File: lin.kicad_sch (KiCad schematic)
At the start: 11 parts, among them J3 Screw_Terminal_01x03, U5 TJA1029T

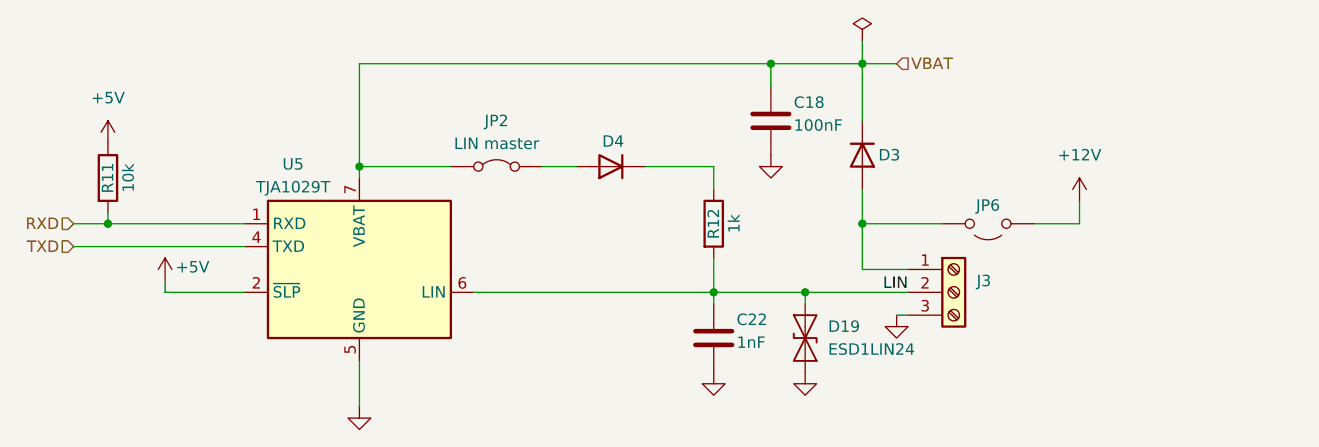
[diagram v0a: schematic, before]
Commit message: Added power diodes
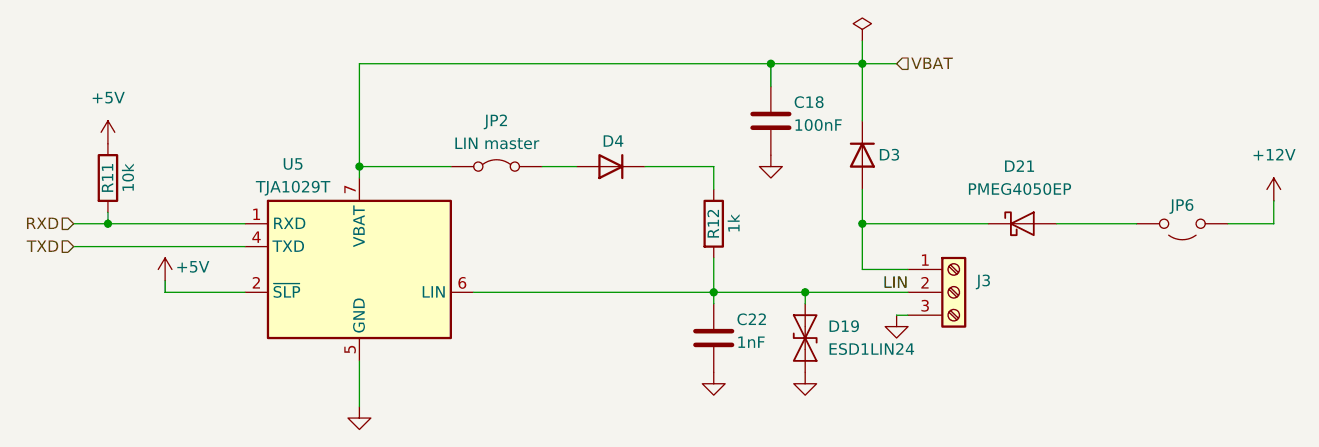
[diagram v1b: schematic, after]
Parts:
- added D21: PMEG4050EP, Diode_SMD:Nexperia_CFP3_SOD-123W, symbol Diode:PMEG4010ER
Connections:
- net at D3.2 (A), J3.1 (Pin_1): now also D21.1 (K); no longer JP6.2 (B)
- new net: D21.2 (A), JP6.2 (B)
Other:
- moved on the sheet: JP6
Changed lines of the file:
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@@
 	(wire
 		(pts
-			(xy 200.66 93.98) (xy 195.58 93.98)
+			(xy 222.25 93.98) (xy 217.17 93.98)
 		)
 		(stroke
@@
 	(wire
 		(pts
-			(xy 200.66 91.44) (xy 200.66 93.98)
+			(xy 222.25 91.44) (xy 222.25 93.98)
 		)
 		(stroke
@@
 	(wire
 		(pts
-			(xy 176.53 93.98) (xy 185.42 93.98)
+			(xy 198.12 93.98) (xy 207.01 93.98)
+		)
+		(stroke
+			(width 0)
+			(type default)
+		)
+	)
+	(wire
+		(pts
+			(xy 176.53 93.98) (xy 190.5 93.98)
 		)
 		(stroke
@@
 	)
 	(symbol
+		(lib_id "Diode:PMEG4010ER")
+		(at 194.31 93.98 0)
+		(unit 1)
+		(exclude_from_sim no)
+		(in_bom yes)
+		(on_board yes)
+		(dnp no)
+		(fields_autoplaced yes)
+		(property "Reference" "D21"
+			(at 193.9925 87.63 0)
+			(effects
+				(font
+					(size 1.27 1.27)
+				)
+			)
+		)
+		(property "Value" "PMEG4050EP"
+			(at 193.9925 90.17 0)
+			(effects
+				(font
+					(size 1.27 1.27)
+				)
+			)
+		)
+		(property "Footprint" "Diode_SMD:Nexperia_CFP3_SOD-123W"
+			(at 194.31 98.425 0)
+			(effects
+				(font
+					(size 1.27 1.27)
+				)
+				(hide yes)
+			)
+		)
+		(property "Datasheet" "https://assets.nexperia.com/documents/data-sheet/PMEG4010ER.pdf"
+			(at 194.31 93.98 0)
+			(effects
+				(font
+					(size 1.27 1.27)
+				)
+				(hide yes)
+			)
+		)
+		(property "Description" "40V, 1A low Vf MEGA Schottky barrier rectifier, SOD-123W"
+			(at 194.31 93.98 0)
+			(effects
+				(font
+					(size 1.27 1.27)
+				)
+				(hide yes)
+			)
+		)
+		(pin "2"
+		)
+		(pin "1"
+		)
+		(instances
+			(project ""
+				(path "/e6cf11d6-0152-4d84-a82a-9e2d93966152/31c6b4ae-10a2-4f10-a591-5579630fa60e"
+					(reference "D22")
+					(unit 1)
+				)
+				(path "/e6cf11d6-0152-4d84-a82a-9e2d93966152/7747294f-2018-4c44-a2cb-fbe0ffa31304"
+					(reference "D24")
+					(unit 1)
+				)
+				(path "/e6cf11d6-0152-4d84-a82a-9e2d93966152/a2f7cee2-a97f-4885-9036-e6c309dcb8d0"
+					(reference "D23")
+					(unit 1)
+				)
+				(path "/e6cf11d6-0152-4d84-a82a-9e2d93966152/ce397451-b7a0-48ce-ab00-72bbf812467b"
+					(reference "D21")
+					(unit 1)
+				)
+			)
+		)
+	)
+	(symbol
 		(lib_id "power:PWR_FLAG")
 		(at 176.53 73.66 0)
@@
 	(symbol
 		(lib_id "Jumper:Jumper_2_Open")
-		(at 190.5 93.98 180)
+		(at 212.09 93.98 180)
 		(unit 1)
 		(exclude_from_sim yes)
@@
 		(dnp no)
 		(property "Reference" "JP6"
-			(at 190.5 91.948 0)
+			(at 212.09 91.948 0)
 			(effects
 				(font
@@
 		)
 		(property "Value" "Jumper_2_Open"
-			(at 190.5 91.44 0)
+			(at 212.09 91.44 0)
 			(effects
 				(font
@@
 		)
 		(property "Footprint" "TestPoint:TestPoint_2Pads_Pitch2.54mm_Drill0.8mm"
-			(at 190.5 93.98 0)
+			(at 212.09 93.98 0)
 			(effects
 				(font
@@
 		)
 		(property "Datasheet" "~"
-			(at 190.5 93.98 0)
+			(at 212.09 93.98 0)
 			(effects
 				(font
@@
 		)
 		(property "Description" "Jumper, 2-pole, open"
-			(at 190.5 93.98 0)
+			(at 212.09 93.98 0)
 			(effects
 				(font
@@
 	(symbol
 		(lib_id "power:+12V")
-		(at 200.66 91.44 0)
+		(at 222.25 91.44 0)
 		(unit 1)
 		(exclude_from_sim no)
@@
 		(fields_autoplaced yes)
 		(property "Reference" "#PWR083"
-			(at 200.66 95.25 0)
+			(at 222.25 95.25 0)
 			(effects
 				(font
@@
 		)
 		(property "Value" "+12V"
-			(at 200.66 86.36 0)
+			(at 222.25 86.36 0)
 			(effects
 				(font
@@
 		)
 		(property "Footprint" ""
-			(at 200.66 91.44 0)
+			(at 222.25 91.44 0)
 			(effects
 				(font
@@
 		)
 		(property "Datasheet" ""
-			(at 200.66 91.44 0)
+			(at 222.25 91.44 0)
 			(effects
 				(font
@@
 		)
 		(property "Description" "Power symbol creates a global label with name \"+12V\""
-			(at 200.66 91.44 0)
-			(effects
-				(font
+			(at 222.25 91.44 0)
+			(effects
+				(font
